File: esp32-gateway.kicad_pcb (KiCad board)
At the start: 2 copper layers, 55 x 95 mm, 43 parts, among them J1 USB_B_Micro, J2 Conn_Coaxial, J3 Ext LED header, J4 Header Left, J5 Header Right, Q1 Q_NPN_BEC, Q2 Q_NPN_BEC, SW1 SW_RESET, SW2 SW_INCLUSION, SW3 SW_GEN1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

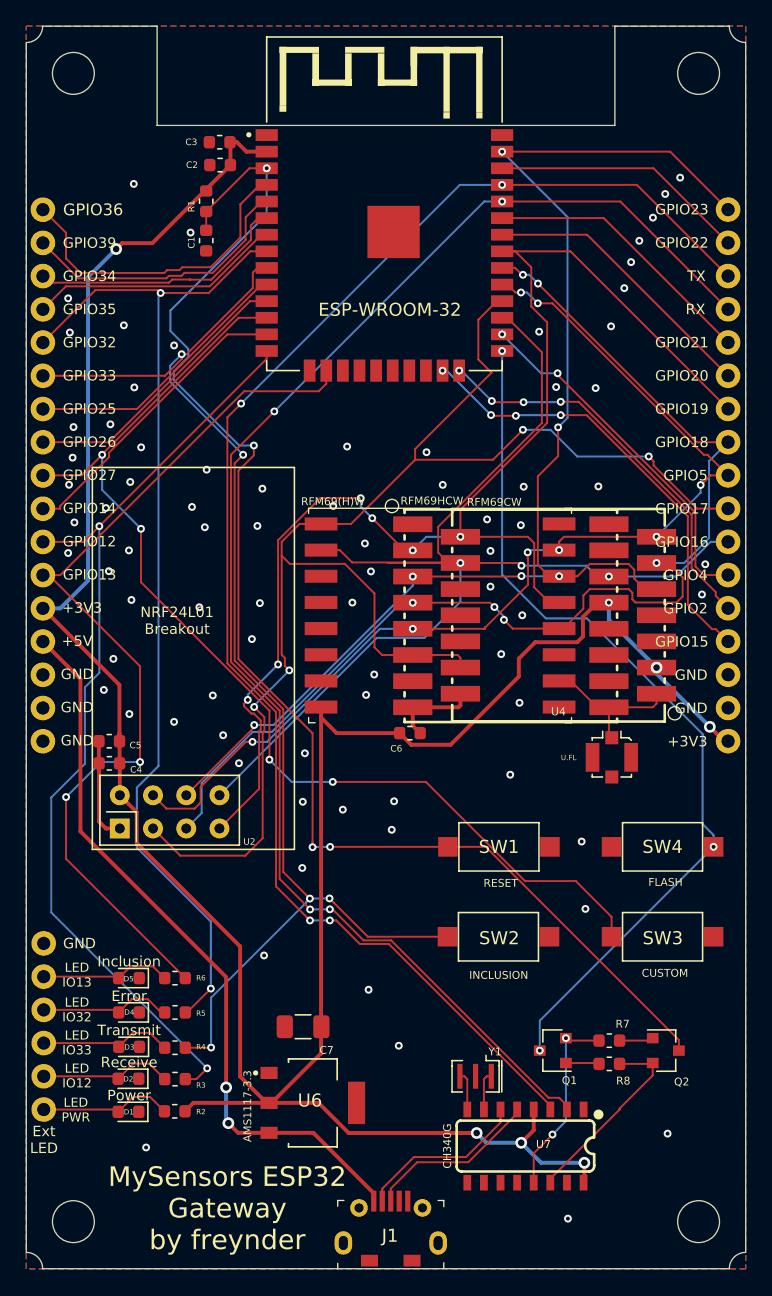
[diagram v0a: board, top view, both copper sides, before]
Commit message: Corrected error and made nicer traces
- inclusion button was connected to IO33, however IO33 was already in
use for transmission led. Connected inclusion button to IO35 instead.
- aligned traces better and maximized ground plane for a nicer board.
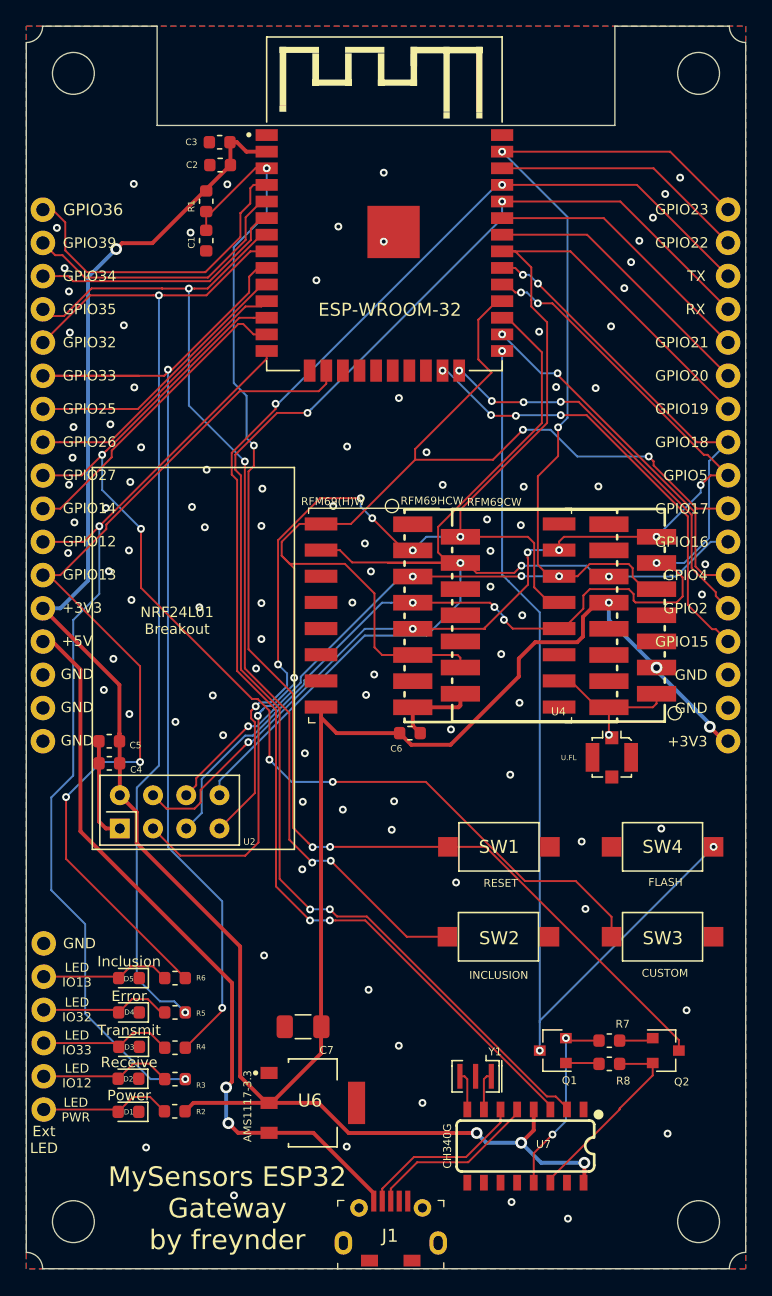
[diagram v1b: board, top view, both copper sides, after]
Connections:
- SW2 pad 1: IO33 -> IO35
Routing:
- net IO35: track 19.5 -> 80.5 mm, vias 0 -> 4
- net IO33: track 96.6 -> 83.4 mm, vias 5 -> 2
- net EN: track 104.4 -> 98.2 mm
- net IO0: track 67.5 -> 73.6 mm
- net ESPTX: track 114.2 -> 112.3 mm
- net IO32: track 79.2 -> 77.7 mm
- net IO16: track 90.9 -> 92.0 mm
- net +5V: track 56.6 -> 57.4 mm
- net IO14: track 23.0 -> 23.6 mm
- net RFMANT: vias 0 -> 1
- net GND: vias 79 -> 94

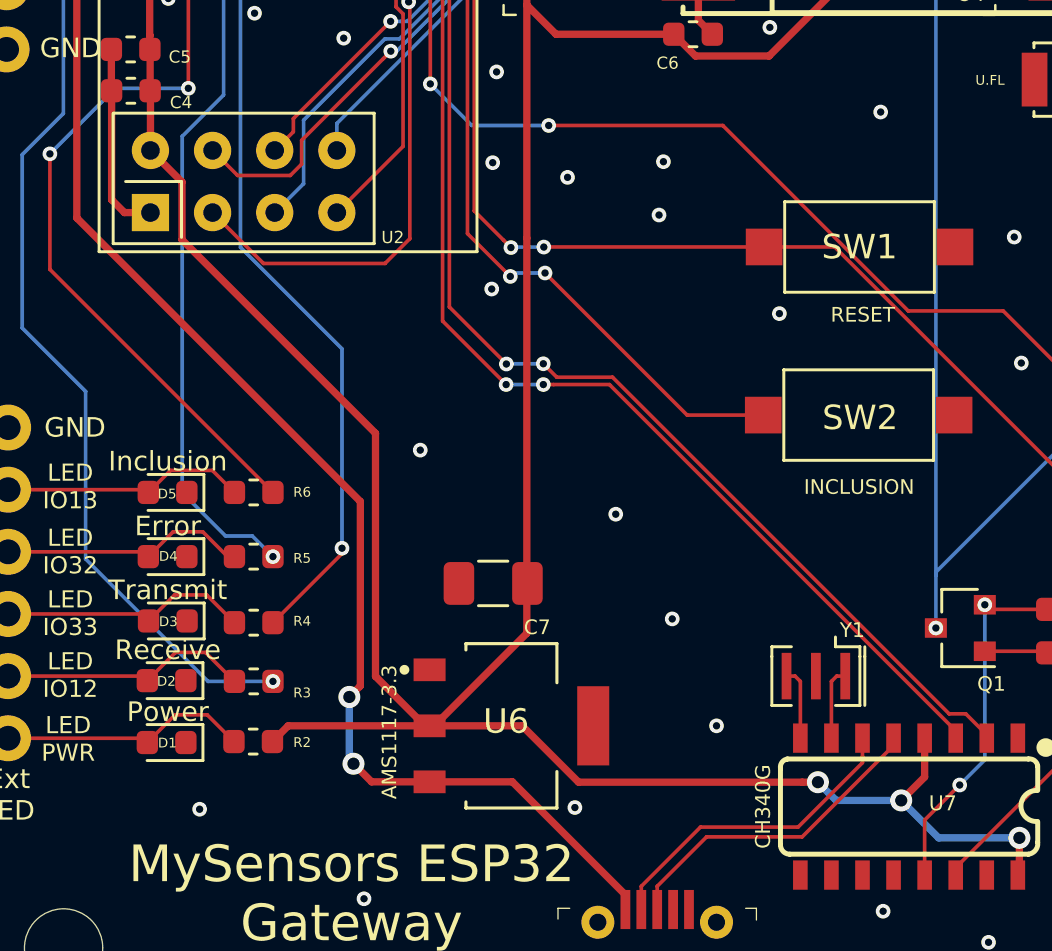
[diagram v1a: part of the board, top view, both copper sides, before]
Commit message: Fixed design error for 3.3v power
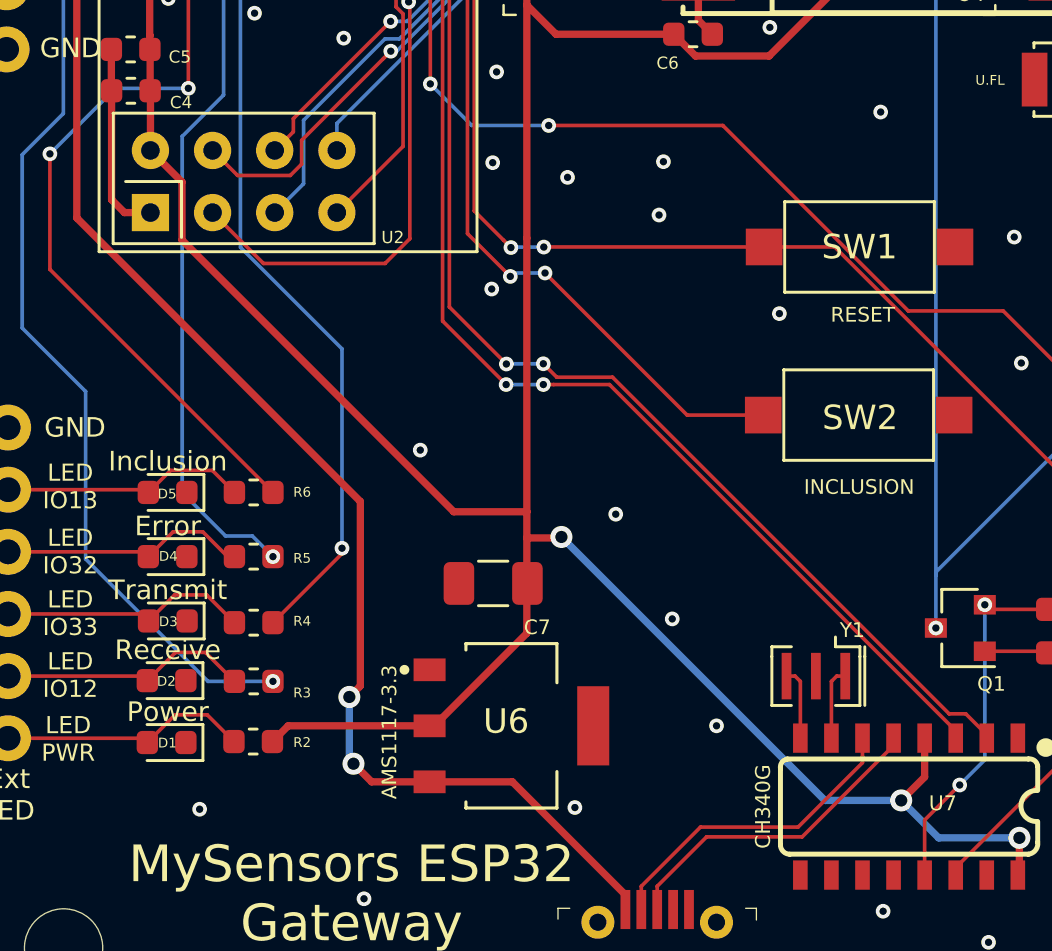
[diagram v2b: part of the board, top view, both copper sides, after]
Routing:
- net +3V3: track 205.5 -> 199.2 mm
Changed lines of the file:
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@@
     (thickness 1.6)
     (drawings 114)
-    (tracks 809)
+    (tracks 806)
     (zones 0)
     (modules 43)
@@
   (segment (start 133.561 147.32) (end 133.751 147.32) (width 0.3) (layer F.Cu) (net 2) (status 30))
   (segment (start 133.751 147.32) (end 137.536 143.535) (width 0.3) (layer F.Cu) (net 2) (status 10))
-  (segment (start 137.536 143.535) (end 137.536 127.381996) (width 0.3) (layer F.Cu) (net 2))
-  (segment (start 131.35 135.36) (end 131.35 145.299) (width 0.3) (layer F.Cu) (net 2))
-  (segment (start 131.35 145.299) (end 133.371 147.32) (width 0.3) (layer F.Cu) (net 2) (status 20))
-  (segment (start 123.44 127.45) (end 131.35 135.36) (width 0.3) (layer F.Cu) (net 2))
-  (segment (start 122.15 123.8) (end 123.44 125.09) (width 0.3) (layer F.Cu) (net 2) (status 10))
-  (segment (start 133.371 147.32) (end 133.561 147.32) (width 0.3) (layer F.Cu) (net 2) (status 30))
-  (segment (start 123.44 125.09) (end 123.44 127.45) (width 0.3) (layer F.Cu) (net 2))
-  (segment (start 149.884309 150.074309) (end 149.43431 149.62431) (width 0.3) (layer B.Cu) (net 2))
-  (segment (start 133.561 147.32) (end 137.345998 147.32) (width 0.3) (layer F.Cu) (net 2) (status 10))
-  (segment (start 139.650308 149.62431) (end 148.797914 149.62431) (width 0.3) (layer F.Cu) (net 2))
-  (segment (start 152.84 150.37) (end 150.18 150.37) (width 0.3) (layer B.Cu) (net 2))
-  (segment (start 137.345998 147.32) (end 139.650308 149.62431) (width 0.3) (layer F.Cu) (net 2))
-  (via (at 149.43431 149.62431) (size 0.9) (drill 0.5) (layers F.Cu B.Cu) (net 2))
-  (segment (start 148.797914 149.62431) (end 149.43431 149.62431) (width 0.3) (layer F.Cu) (net 2))
-  (segment (start 150.18 150.37) (end 149.884309 150.074309) (width 0.3) (layer B.Cu) (net 2))
   (segment (start 137.536 127.381996) (end 137.536 117.858) (width 0.3) (layer F.Cu) (net 2))
   (segment (start 163.186 114.276) (end 163.186 114.038) (width 0.3) (layer B.Cu) (net 2))
   (segment (start 167.26 118.57) (end 167.26 118.35) (width 0.3) (layer B.Cu) (net 2))
   (segment (start 167.26 118.35) (end 163.186 114.276) (width 0.3) (layer B.Cu) (net 2))
+  (via (at 138.95 139.6) (size 0.9) (drill 0.5) (layers F.Cu B.Cu) (net 2))
+  (segment (start 138.91 139.64) (end 138.95 139.6) (width 0.3) (layer F.Cu) (net 2))
+  (segment (start 137.536 139.64) (end 138.91 139.64) (width 0.3) (layer F.Cu) (net 2))
+  (segment (start 137.536 143.535) (end 137.536 139.64) (width 0.3) (layer F.Cu) (net 2))
+  (segment (start 149.72 150.37) (end 152.84 150.37) (width 0.3) (layer B.Cu) (net 2))
+  (segment (start 138.95 139.6) (end 149.72 150.37) (width 0.3) (layer B.Cu) (net 2))
+  (segment (start 137.536 138.57) (end 134.55 138.57) (width 0.3) (layer F.Cu) (net 2))
+  (segment (start 137.536 138.57) (end 137.536 127.381996) (width 0.3) (layer F.Cu) (net 2))
+  (segment (start 137.536 139.64) (end 137.536 138.57) (width 0.3) (layer F.Cu) (net 2))
+  (segment (start 134.55 138.57) (end 123.44 127.46) (width 0.3) (layer F.Cu) (net 2))
+  (segment (start 123.44 125.09) (end 122.15 123.8) (width 0.3) (layer F.Cu) (net 2))
+  (segment (start 123.44 127.46) (end 123.44 125.09) (width 0.3) (layer F.Cu) (net 2))
   (via (at 130.28 146.14) (size 0.9) (drill 0.5) (layers F.Cu B.Cu) (net 3))
   (via (at 130.45 148.87) (size 0.9) (drill 0.5) (layers F.Cu B.Cu) (net 3))
